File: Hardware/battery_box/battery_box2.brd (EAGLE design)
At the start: 60 x 80.1 mm, 49 parts, among them IC1 AD826R, IC2 LM2574, IC3 PIC16F1824, IC4 LD117AS18TR, J1 CON_HEADER_PRG_PIC_ICSPA, Q1 IRFR5505PBFTO252, Q2 BSS123, X1 CON_MOLEX_39_29_1028, X2 KUSBVX

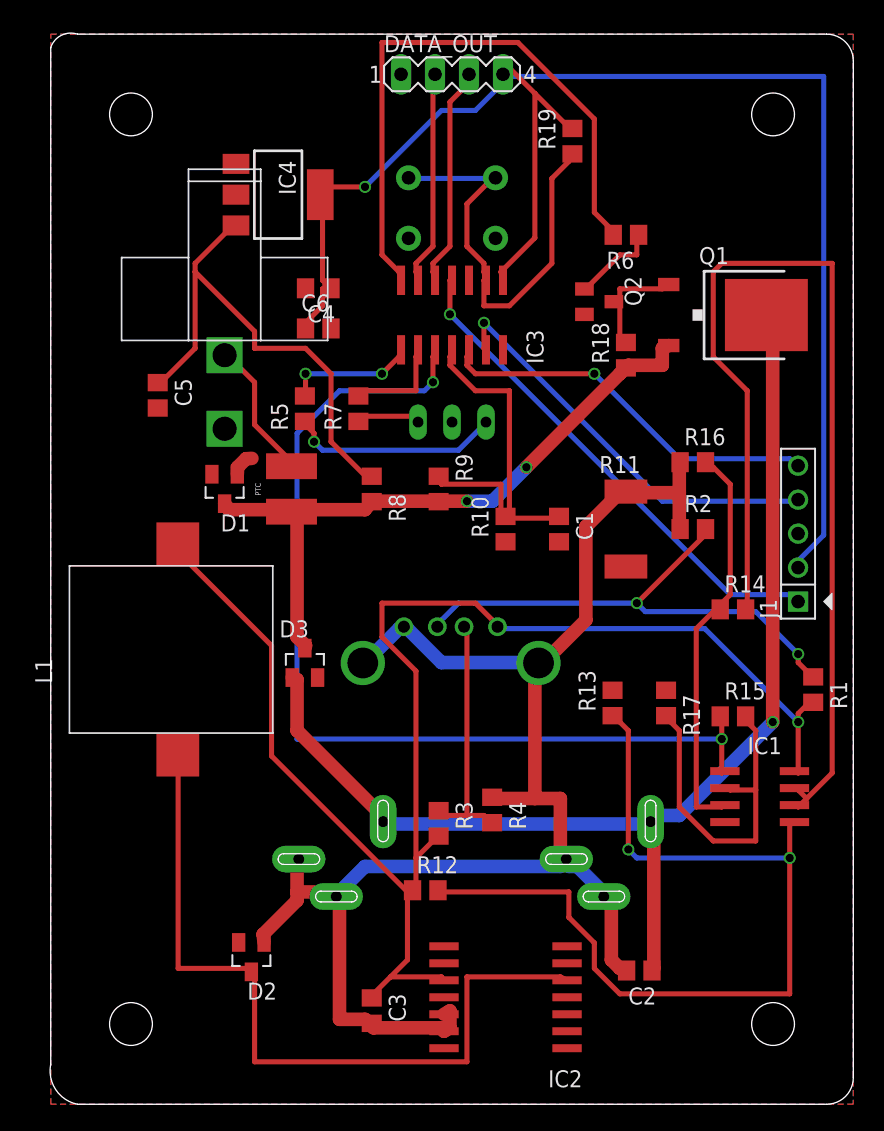
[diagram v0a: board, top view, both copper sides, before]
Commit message: Cleaned up and routed PCB and Schematic files
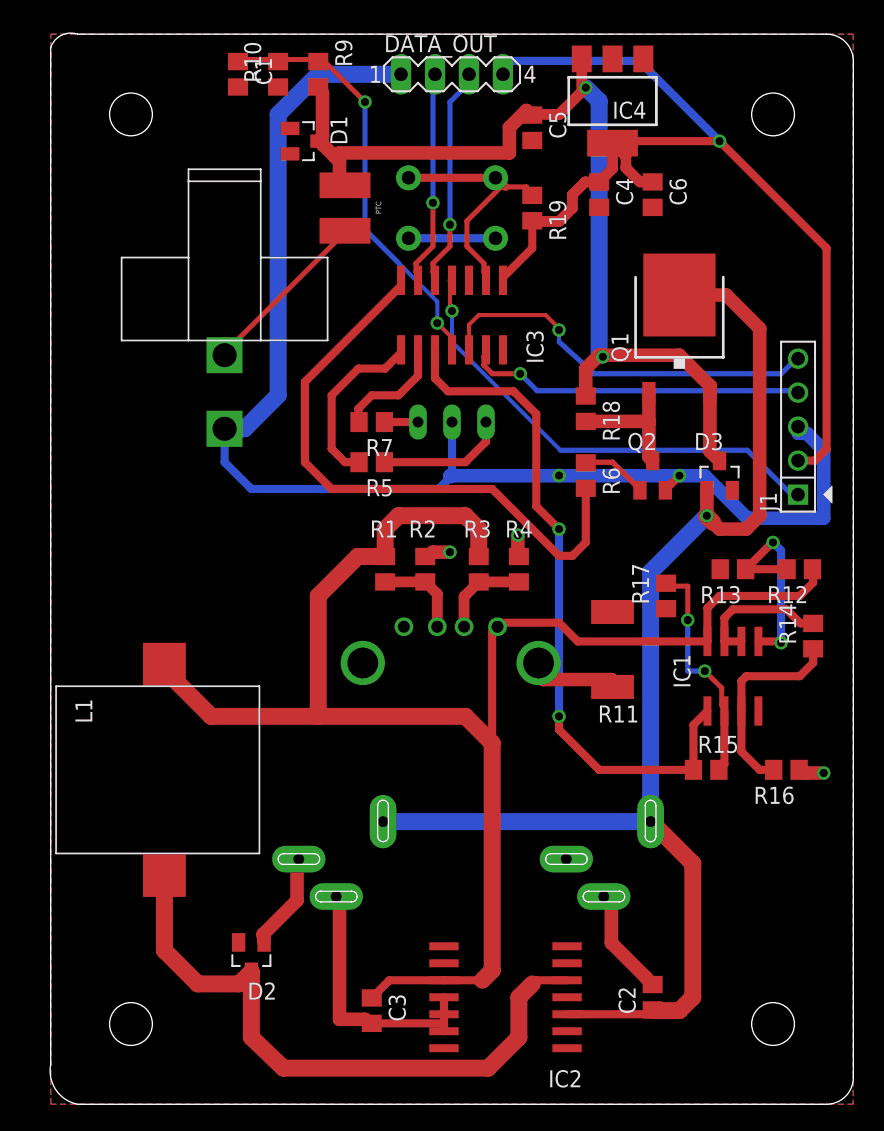
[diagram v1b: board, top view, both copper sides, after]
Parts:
- removed R8: 500, rcl:R0805
- moved C1 41.6 mm to (14.0, 77.0)
- moved R10 38.0 mm to (17.0, 77.0)
- moved R12 36.9 mm to (56.0, 40.0), turned to 180 degrees
- moved C5 34.4 mm to (36.0, 73.0)
- moved D3 34.0 mm to (50.0, 47.0)
- moved R1 33.2 mm to (25.0, 40.0), turned to 90 degrees
- moved R9 32.3 mm to (20.0, 77.0)
- moved C6 26.9 mm to (45.0, 68.0), turned to 270 degrees
- moved D1 26.7 mm to (19.0, 72.0), turned to 270 degrees
- moved IC4 26.0 mm to (42.0, 75.0), turned to 180 degrees
- moved R16 24.0 mm to (55.0, 25.0), turned to 180 degrees
- moved C4 22.1 mm to (41.0, 68.0), turned to 270 degrees
- moved U$2 21.4 mm to (22.0, 67.0), turned to 270 degrees
- moved R2 20.2 mm to (28.0, 40.0), turned to 270 degrees
- moved R3 19.2 mm to (32.0, 40.0), turned to 90 degrees
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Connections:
- net N$1 renamed 12V_OUT
- net N$20 renamed GND_OUTPUT
- removed net N$13: C5.1, IC4.3, R8.1
- net V_BATT: now also C5.1, IC4.3; no longer R8.2
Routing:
- net GND: track 1.86 -> 114.8 mm, vias 0 -> 2
- net GND_OUTPUT: track 119.9 -> 47.6 mm, vias 0 -> 3
- net N$19: track 78.7 -> 10.4 mm
- net N$17: track 67.6 -> 15.5 mm
- net N$13: track 37.6 -> 0.00 mm
- net VDD: track 113.3 -> 76.6 mm
- net N$3: track 39.2 -> 6.72 mm, vias 2 -> 0
- net V_BATT: track 49.9 -> 76.4 mm
- net I_SENSE: track 73.3 -> 51.2 mm
- net N$15: track 30.0 -> 15.2 mm
- net POW: track 32.9 -> 18.8 mm
- net N$5: track 18.6 -> 6.81 mm
- net N$9: track 58.1 -> 47.4 mm
- net 12V_OUT: track 87.9 -> 96.8 mm
- net N$16: track 25.9 -> 17.4 mm, vias 0 -> 2
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- added copper zone on layer 16, net GND_OUTPUT
- removed copper zone on layer 16, net GND
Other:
- board text removed: "Cap C2 needs to be closer to the LM2574"

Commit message: Added new components with correct footprints
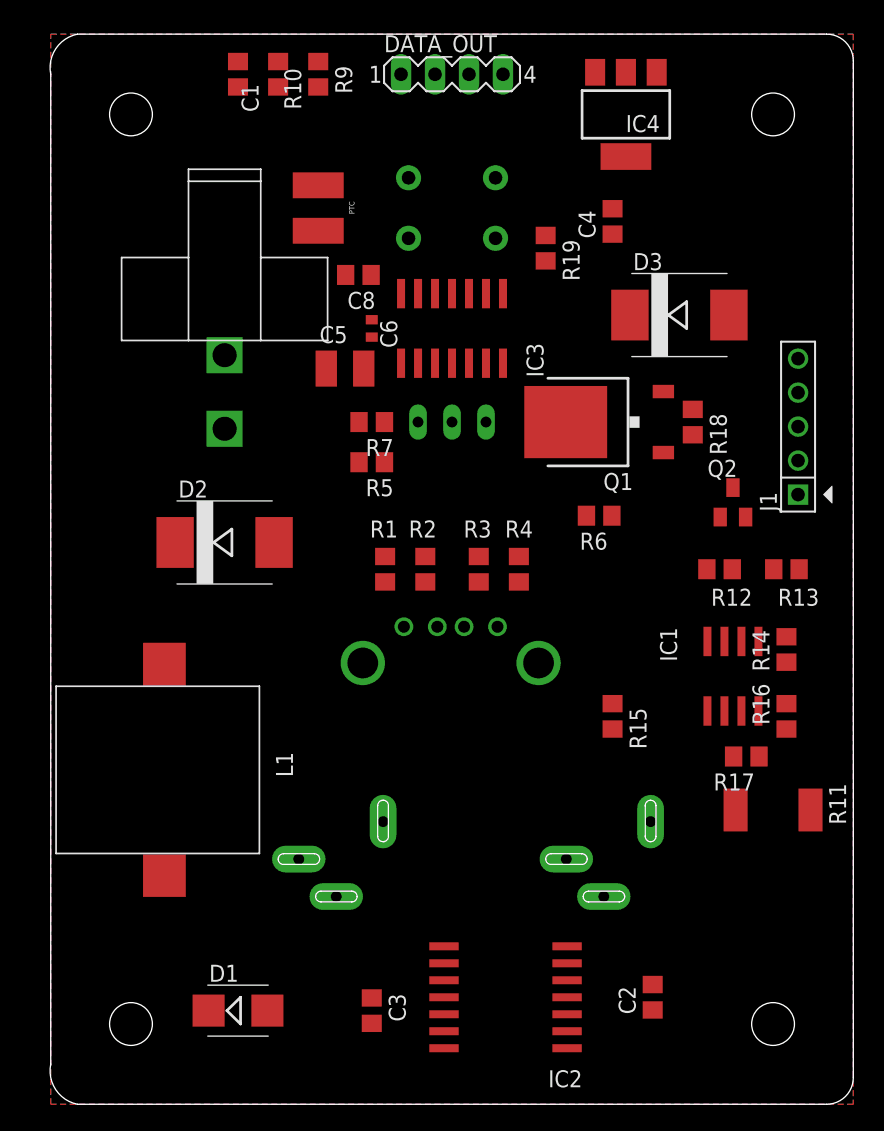
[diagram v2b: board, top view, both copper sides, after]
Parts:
- added C8: 10u, 6.3V, rcl:C0805
- C5: value (none) -> 10u, 25V; device rcl:C0805 -> rcl:C1210
- C6: device rcl:C0805 -> rcl:C0402
- D1: value BAS40 -> (none); device diode:SOT23 -> diode:SMB
- D2, D3: value BAS40 -> (none); device diode:SOT23 -> diode:SMC
- moved D1 65.2 mm to (14.0, 7.00), turned to 0 degrees
- moved D2 31.1 mm to (13.0, 42.0), turned to 0 degrees
- moved C6 23.3 mm to (24.0, 58.0)
- moved C5 22.8 mm to (22.0, 55.0), turned to 0 degrees
- moved R11 17.0 mm to (54.0, 22.0), turned to 0 degrees
- moved R17 13.4 mm to (52.0, 26.0), turned to 180 degrees
- moved D3 12.4 mm to (47.0, 59.0)
- moved Q1 9.22 mm to (41.0, 51.0), turned to 90 degrees
- moved R15 8.06 mm to (42.0, 29.0), turned to 270 degrees
- moved R18 8.06 mm to (48.0, 51.0)
- moved Q2 6.32 mm to (51.0, 45.0)
- moved R12 6.00 mm to (50.0, 40.0), turned to 0 degrees
- moved R13 4.00 mm to (55.0, 40.0), turned to 0 degrees
- moved R16 4.00 mm to (55.0, 29.0), turned to 90 degrees
- moved R19 3.16 mm to (37.0, 64.0)
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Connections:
- net 12V_OUT: now also D2.A; no longer D3.1
- net GND: now also C8.2, D3.A; no longer D1.1
- net GND_OUTPUT: now also D1.A; no longer D2.1
- net N$9: now also D1.C; no longer D2.3
- net VDD: now also C8.1
- net V_BATT: now also D2.C, D3.C; no longer D1.3, D3.3
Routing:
- net USB_OUT: track 118.7 -> 0.00 mm
- net GND: track 114.8 -> 0.00 mm, vias 2 -> 0
- net 12V_OUT: track 96.8 -> 0.00 mm, vias 1 -> 0
- net VDD: track 76.6 -> 0.00 mm, vias 1 -> 0
- net V_BATT: track 76.4 -> 0.00 mm, vias 2 -> 0
- net I_SENSE: track 51.2 -> 0.00 mm, vias 2 -> 0
- net GND_OUTPUT: track 47.6 -> 0.00 mm, vias 3 -> 0
- net N$9: track 47.4 -> 0.00 mm
- net N$14: track 44.9 -> 0.00 mm
- net MCLR_: track 35.7 -> 0.00 mm, vias 1 -> 0
- net N$8: track 32.2 -> 0.00 mm, vias 2 -> 0
- net PGC: track 29.5 -> 0.00 mm, vias 1 -> 0
- net PGD: track 25.5 -> 0.00 mm, vias 1 -> 0
- net POW: track 18.8 -> 0.00 mm
- net N$16: track 17.4 -> 0.00 mm, vias 2 -> 0
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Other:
- board size 60 x 80.1 mm -> 60 x 80 mm

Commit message: Re-routed PCB
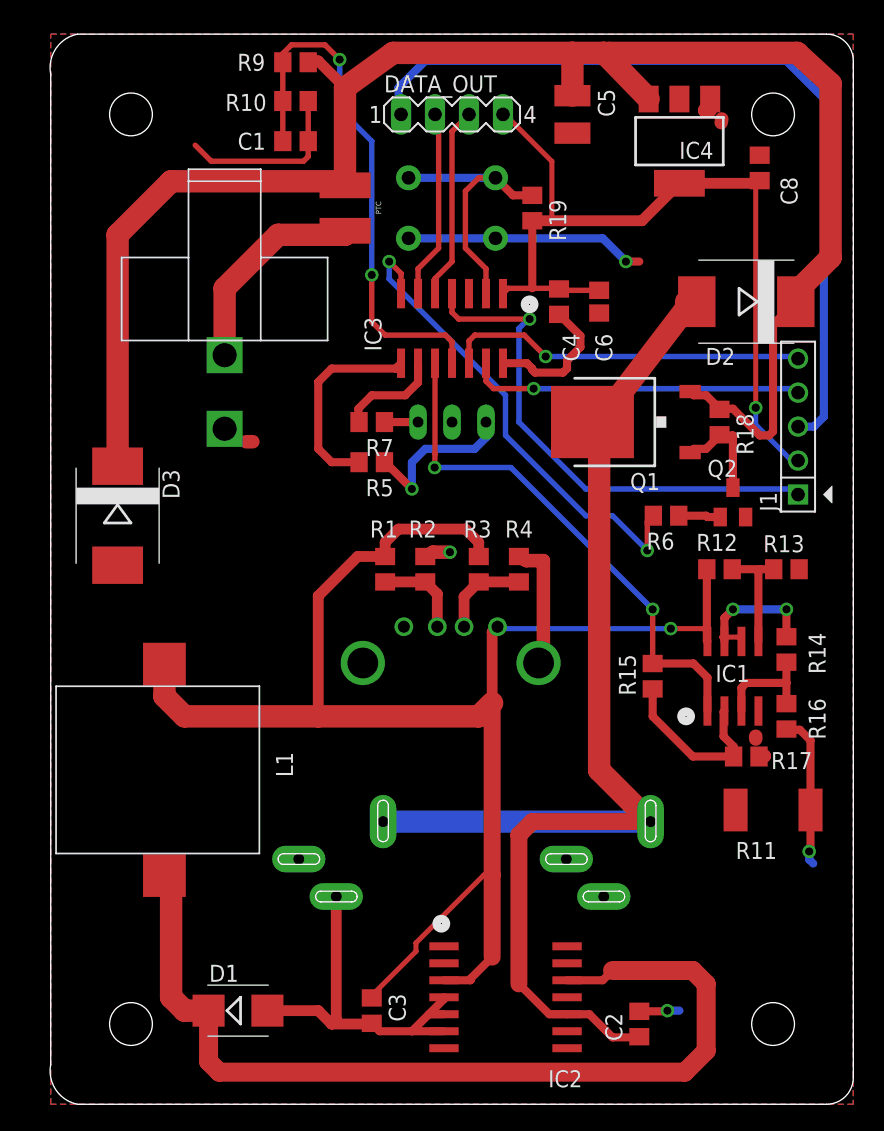
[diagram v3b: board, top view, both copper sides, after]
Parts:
- C6: device rcl:C0402 -> resistor:C0805
- moved D3 44.6 mm to (5.00, 44.0), turned to 270 degrees
- moved D2 43.0 mm to (52.0, 60.0), turned to 180 degrees
- moved C8 31.0 mm to (53.0, 70.0), turned to 90 degrees
- moved C5 25.5 mm to (39.0, 74.0), turned to 270 degrees
- moved C6 17.1 mm to (41.0, 60.0)
- moved C4 7.21 mm to (38.0, 60.0), turned to 270 degrees
- moved C1 6.59 mm to (18.3, 72.0), turned to 0 degrees
- moved R6 5.00 mm to (46.0, 44.0)
- moved IC4 4.47 mm to (47.0, 72.0)
- moved R15 4.24 mm to (45.0, 32.0)
- moved R19 3.16 mm to (36.0, 67.0)
- moved DATA_OUT 3.00 mm to (30.0, 74.0)
- moved R10 2.39 mm to (18.3, 75.0), turned to 180 degrees
- moved C2 2.24 mm to (44.0, 6.00)
- moved Q1 2.00 mm to (43.0, 51.0)
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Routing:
- net V_BATT: track 0.00 -> 129.5 mm
- net USB_OUT: track 0.00 -> 117.5 mm, vias 0 -> 1
- net GND: track 0.00 -> 108.3 mm, vias 0 -> 1
- net 12V_OUT: track 0.00 -> 97.2 mm
- net N$9: track 0.00 -> 70.6 mm
- net VDD: track 0.00 -> 62.8 mm, vias 0 -> 1
- net GND_OUTPUT: track 0.00 -> 54.6 mm, vias 0 -> 3
- net N$8: track 0.00 -> 40.3 mm, vias 0 -> 2
- net I_SENSE: track 0.00 -> 39.6 mm, vias 0 -> 2
- net MCLR_: track 0.00 -> 38.6 mm, vias 0 -> 1
- net N$14: track 0.00 -> 36.3 mm, vias 0 -> 2
- net PGC: track 0.00 -> 27.2 mm, vias 0 -> 1
- net PGD: track 0.00 -> 25.0 mm, vias 0 -> 1
- net POW: track 0.00 -> 20.8 mm
- net N$6: track 0.00 -> 16.0 mm
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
